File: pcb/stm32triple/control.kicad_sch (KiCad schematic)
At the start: 30 parts, among them J1 USB_C_Receptacle_USB2.0, P1 FTSH-107-01-L-DV-K, P2 ST-Link, P3 AFC07-S24FCC-00, SW1 RotaryEncoder_Switch, U1 STM32G431CBUx, U2 TPS82130, U3 BME680, U7 TSOP312xx, U8 TSOP312xx

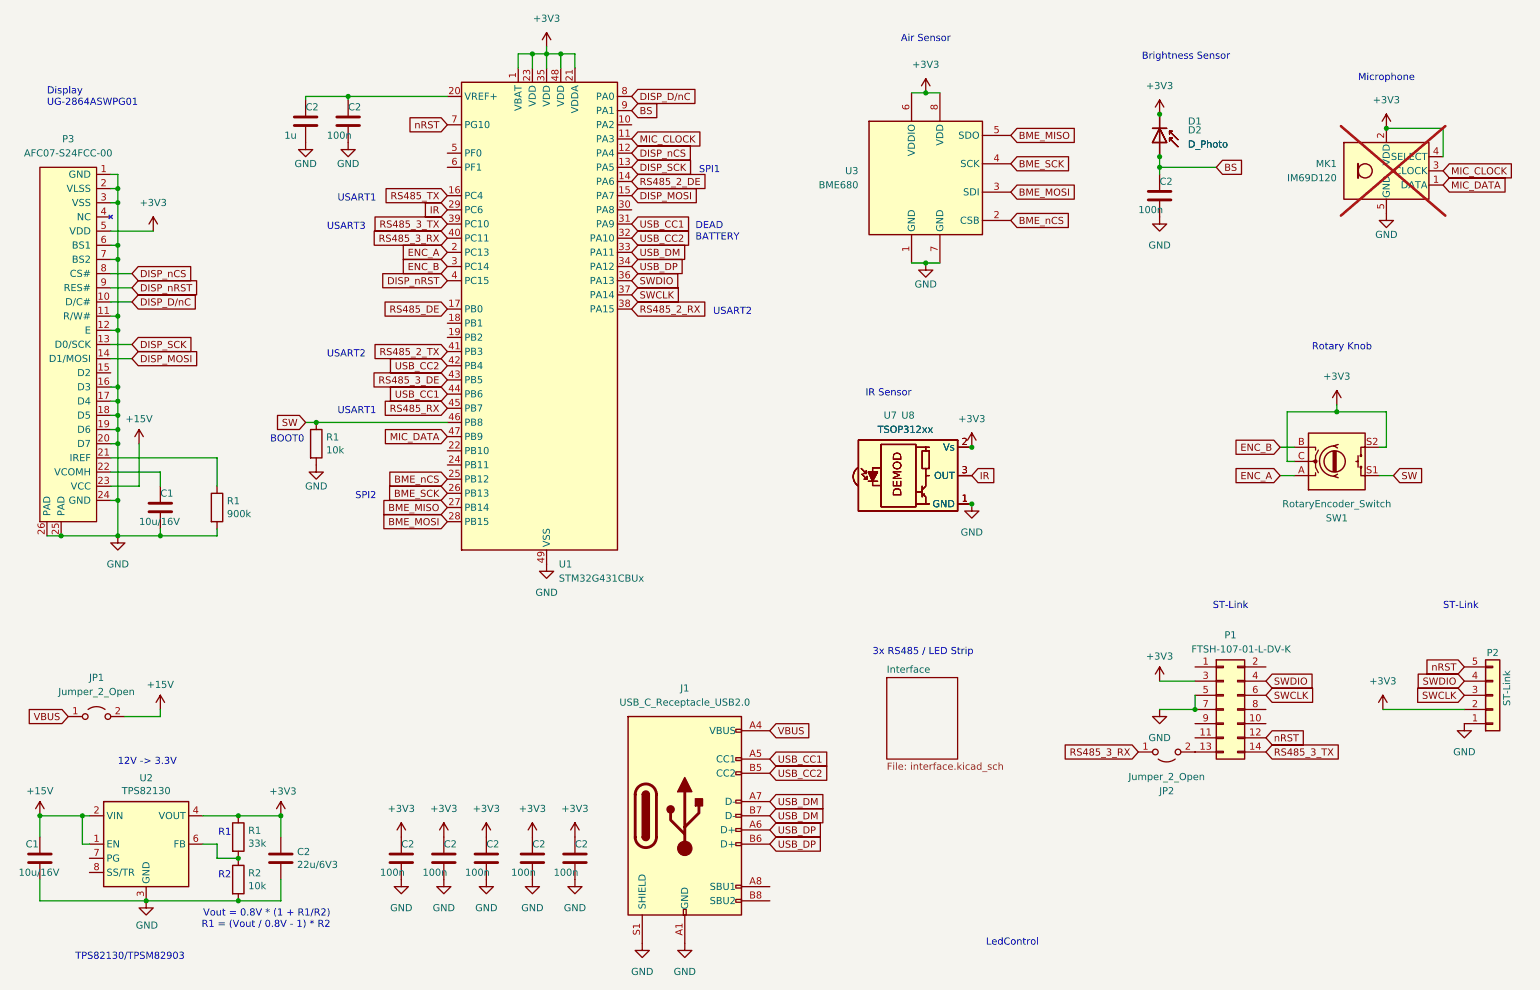
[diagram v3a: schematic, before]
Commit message: Use TSOP38338
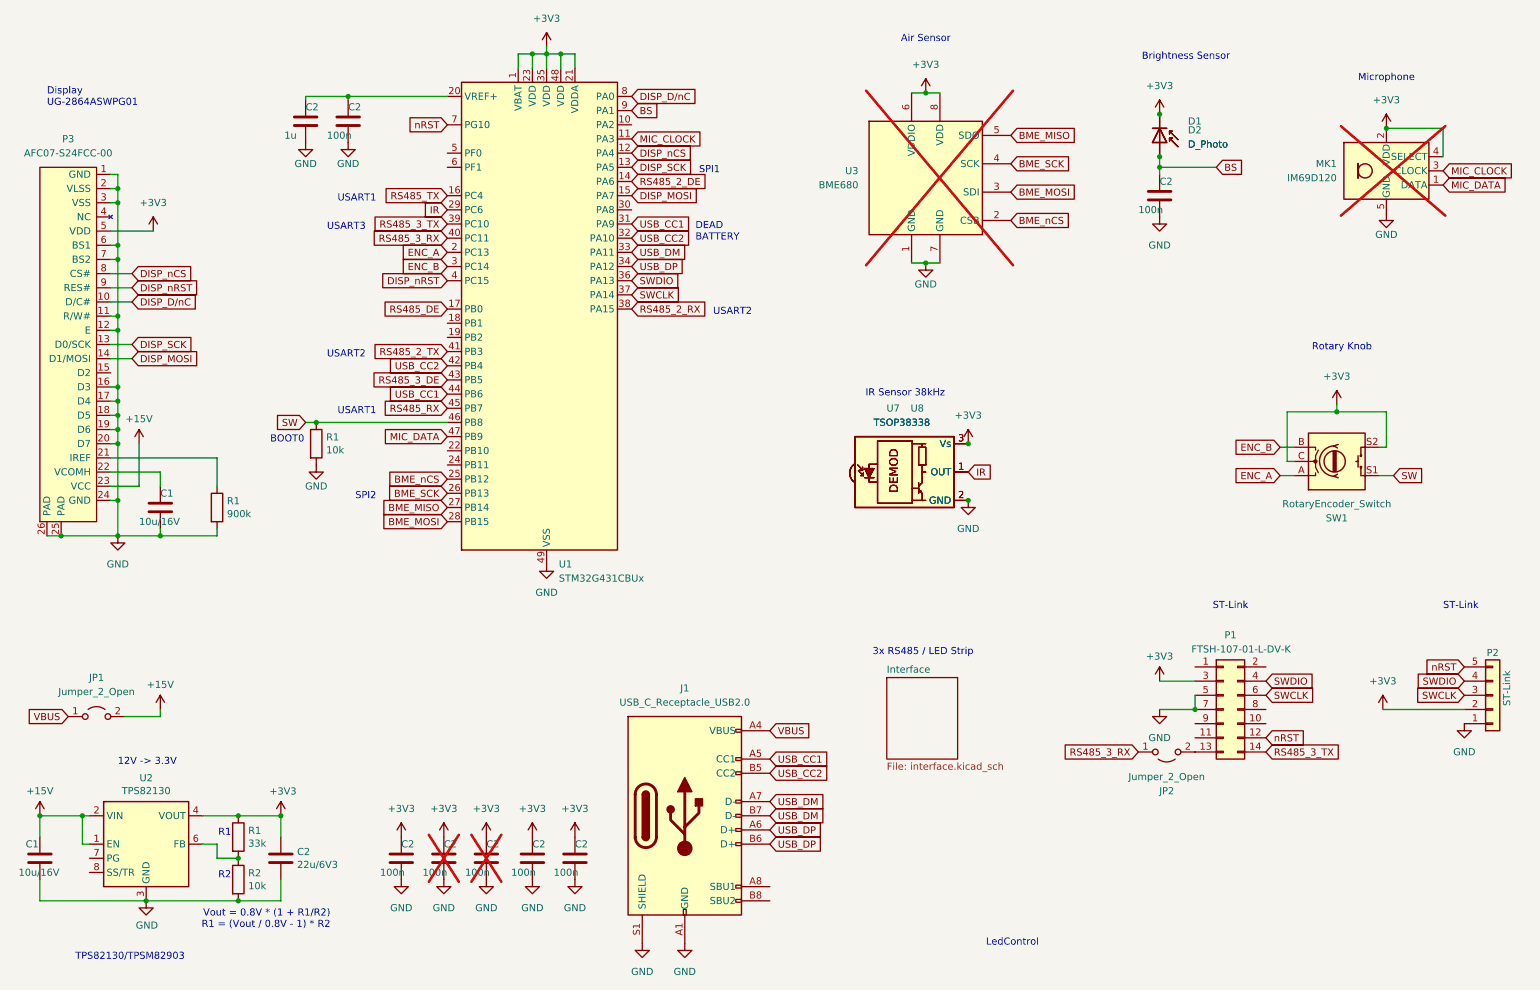
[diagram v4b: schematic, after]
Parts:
- removed U7, U8: TSOP312xx, local:TSOP31238, symbol Interface_Optical:TSOP312xx
- added U7, U8: TSOP38338, local:TSOP38338, symbol Interface_Optical:TSOP382xx
- C2: now not fitted
- J1: footprint local:USB4105-GF-A-120 -> local:TYPE-C-16PIN-2MD-073
- U1: footprint local:STM32G431CBU -> local:STM32-UFQFPN48
- U3: now not fitted; now in the parts list
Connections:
- net +3V3: now also U7.3 (Vs), U8.3 (Vs)
- net GND: now also U7.2 (GND), U8.2 (GND)
- net IR: now also U7.1 (OUT), U8.1 (OUT)
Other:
- note added: "IR Sensor 38kHz"
- note removed: "IR Sensor"
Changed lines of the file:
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@@
 	)
 	(junction
-		(at 186.055 111.125)
+		(at 19.05 167.005)
 		(diameter 0)
 		(color 0 0 0 0)
 	)
 	(junction
-		(at 19.05 167.005)
+		(at 219.71 48.895)
 		(diameter 0)
 		(color 0 0 0 0)
 	)
 	(junction
-		(at 219.71 48.895)
+		(at 185.42 110.49)
 		(diameter 0)
 		(color 0 0 0 0)
@@
 	)
 	(junction
-		(at 54.61 182.245)
+		(at 185.42 100.33)
 		(diameter 0)
 		(color 0 0 0 0)
 	)
 	(junction
-		(at 54.61 167.005)
+		(at 54.61 182.245)
 		(diameter 0)
 		(color 0 0 0 0)
 	)
 	(junction
-		(at 112.395 30.48)
+		(at 54.61 167.005)
 		(diameter 0)
 		(color 0 0 0 0)
 	)
 	(junction
-		(at 186.055 100.965)
+		(at 112.395 30.48)
 		(diameter 0)
 		(color 0 0 0 0)
@@
 		)
 	)
-	(text "IR Sensor"
+	(text "IR Sensor 38kHz"
 		(exclude_from_sim no)
 		(at 167.005 92.075 0)
@@
 	(global_label "IR"
 		(shape input)
-		(at 186.055 106.045 0)
+		(at 185.42 105.41 0)
 		(fields_autoplaced yes)
 		(effects
@@
 		)
 		(property "Intersheetrefs" "${INTERSHEET_REFS}"
-			(at 190.915 106.045 0)
+			(at 190.28 105.41 0)
 			(effects
 				(font
@@
 		(unit 1)
 		(exclude_from_sim no)
-		(in_bom no)
+		(in_bom yes)
 		(on_board yes)
-		(dnp no)
+		(dnp yes)
 		(fields_autoplaced yes)
 		(property "Reference" "U3"
@@
 	(symbol
 		(lib_id "power:GND")
-		(at 186.055 111.125 0)
+		(at 185.42 110.49 0)
 		(unit 1)
 		(exclude_from_sim no)
@@
 		(fields_autoplaced yes)
 		(property "Reference" "#PWR010"
-			(at 186.055 117.475 0)
+			(at 185.42 116.84 0)
 			(effects
 				(font
@@
 		)
 		(property "Value" "GND"
-			(at 186.055 116.205 0)
+			(at 185.42 115.57 0)
 			(effects
 				(font
@@
 		)
 		(property "Footprint" ""
-			(at 186.055 111.125 0)
+			(at 185.42 110.49 0)
 			(effects
 				(font
@@
 		)
 		(property "Datasheet" ""
-			(at 186.055 111.125 0)
+			(at 185.42 110.49 0)
 			(effects
 				(font
@@
 		)
 		(property "Description" ""
-			(at 186.055 111.125 0)
+			(at 185.42 110.49 0)
 			(effects
 				(font
@@
 			)
 		)
-		(property "Footprint" "local:STM32G431CBU"
+		(property "Footprint" "local:STM32-UFQFPN48"
 			(at 94.615 119.38 0)
 			(effects
@@
 		(in_bom yes)
 		(on_board yes)
-		(dnp no)
+		(dnp yes)
 		(property "Reference" "C2"
 			(at 91.44 172.085 0)
@@
 		(in_bom yes)
 		(on_board yes)
-		(dnp no)
+		(dnp yes)
 		(property "Reference" "C2"
 			(at 99.06 172.085 0)
@@
 	(symbol
 		(lib_id "power:+3V3")
-		(at 186.055 100.965 0)
+		(at 185.42 100.33 0)
 		(unit 1)
 		(exclude_from_sim no)
@@
 		(fields_autoplaced yes)
 		(property "Reference" "#PWR02"
-			(at 186.055 104.775 0)
+			(at 185.42 104.14 0)
 			(effects
 				(font
@@
 		)
 		(property "Value" "+3V3"
-			(at 186.055 95.885 0)
+			(at 185.42 95.25 0)
 			(effects
 				(font
@@
 		)
 		(property "Footprint" ""
-			(at 186.055 100.965 0)
+			(at 185.42 100.33 0)
 			(effects
 				(font
@@
 		)
 		(property "Datasheet" ""
-			(at 186.055 100.965 0)
+			(at 185.42 100.33 0)
 			(effects
 				(font
@@
 		)
 		(property "Description" ""
-			(at 186.055 100.965 0)
+			(at 185.42 100.33 0)
 			(effects
 				(font
@@
 	)
 	(symbol
+		(lib_id "Interface_Optical:TSOP382xx")
+		(at 175.26 105.41 0)
+		(unit 1)
+		(exclude_from_sim no)
+		(in_bom yes)
+		(on_board yes)
+		(dnp no)
+		(property "Reference" "U8"
+			(at 176.276 93.98 0)
+			(effects
+				(font
+					(size 1.27 1.27)
+				)
+			)
+		)
+		(property "Value" "TSOP38338"
+			(at 173.525 96.52 0)
+			(effects
+				(font
+					(size 1.27 1.27)
+				)
+			)
+		)
+		(property "Footprint" "local:TSOP38338"
+			(at 173.99 114.935 0)
+			(effects
+				(font
+					(size 1.27 1.27)
+				)
+				(hide yes)
+			)
+		)
+		(property "Datasheet" "http://www.vishay.com/docs/82491/tsop382.pdf"
+			(at 191.77 97.79 0)
+			(effects
+				(font
+					(size 1.27 1.27)
+				)
+				(hide yes)
+			)
+		)
+		(property "Description" "Photo Modules for PCM Remote Control Systems"
+			(at 175.26 105.41 0)
+			(effects
+				(font
+					(size 1.27 1.27)
+				)
+				(hide yes)
+			)
+		)
+		(pin "3"
+		)
+		(pin "1"
+		)
+		(pin "2"
+		)
+		(instances
+			(project "control"
+				(path "/4b540715-c4ed-4902-8525-92fb403f6b2e"
+					(reference "U8")
+					(unit 1)
+				)
+			)
+		)
+	)
+	(symbol
 		(lib_id "Connector_Generic:Conn_01x05")
 		(at 279.4 145.415 0)
@@
 	)
 	(symbol
-		(lib_id "Interface_Optical:TSOP312xx")
-		(at 175.895 106.045 0)
-		(unit 1)
-		(exclude_from_sim no)
-		(in_bom no)
-		(on_board yes)
-		(dnp no)
-		(property "Reference" "U7"
-			(at 171.45 95.25 0)
-			(effects
-				(font
-					(size 1.27 1.27)
-				)
-			)
-		)
-		(property "Value" "TSOP312xx"
-			(at 174.16 97.79 0)
-			(effects
-				(font
-					(size 1.27 1.27)
-				)
-			)
-		)
-		(property "Footprint" "local:TSOP31238"
-			(at 174.625 115.57 0)
-			(effects
-				(font
-					(size 1.27 1.27)
-				)
-				(hide yes)
-			)
-		)
-		(property "Datasheet" "http://www.vishay.com/docs/82492/tsop312.pdf"
-			(at 192.405 98.425 0)
-			(effects
-				(font
-					(size 1.27 1.27)
-				)
-				(hide yes)
-			)
-		)
-		(property "Description" ""
-			(at 175.895 106.045 0)
-			(effects
-				(font
-					(size 1.27 1.27)
-				)
-				(hide yes)
-			)
-		)
-		(pin "1"
-		)
-		(pin "2"
-		)
-		(pin "3"
-		)
-		(instances
-			(project "control"
-				(path "/4b540715-c4ed-4902-8525-92fb403f6b2e"
-					(reference "U7")
-					(unit 1)
-				)
-			)
-		)
-	)
-	(symbol
 		(lib_id "Device:C")
 		(at 62.23 174.625 0)
@@
 	)
 	(symbol
-		(lib_id "Interface_Optical:TSOP312xx")
-		(at 175.895 106.045 0)
+		(lib_id "Interface_Optical:TSOP382xx")
+		(at 175.26 105.41 0)
 		(unit 1)
 		(exclude_from_sim no)
-		(in_bom no)
+		(in_bom yes)
 		(on_board yes)
 		(dnp no)
-		(property "Reference" "U8"
-			(at 174.625 95.25 0)
+		(property "Reference" "U7"
+			(at 171.958 93.98 0)
 			(effects
 				(font
@@
 			)
 		)
-		(property "Value" "TSOP312xx"
-			(at 174.16 97.79 0)
+		(property "Value" "TSOP38338"
+			(at 173.525 96.52 0)
 			(effects
 				(font
@@
 			)
 		)
-		(property "Footprint" "local:TSOP31238"
-			(at 174.625 115.57 0)
+		(property "Footprint" "local:TSOP38338"
+			(at 173.99 114.935 0)
 			(effects
 				(font
@@
 			)
 		)
-		(property "Datasheet" "http://www.vishay.com/docs/82492/tsop312.pdf"
-			(at 192.405 98.425 0)
+		(property "Datasheet" "http://www.vishay.com/docs/82491/tsop382.pdf"
+			(at 191.77 97.79 0)
 			(effects
 				(font
@@
 			)
 		)
-		(property "Description" ""
-			(at 175.895 106.045 0)
+		(property "Description" "Photo Modules for PCM Remote Control Systems"
+			(at 175.26 105.41 0)
 			(effects
 				(font
@@
 			)
 		)
+		(pin "3"
+		)
 		(pin "1"
 		)
 		(pin "2"
 		)
-		(pin "3"
-		)
 		(instances
-			(project "control"
+			(project ""
 				(path "/4b540715-c4ed-4902-8525-92fb403f6b2e"
-					(reference "U8")
+					(reference "U7")
 					(unit 1)
 				)
@@
 			)
 		)
-		(property "Footprint" "local:USB4105-GF-A-120"
+		(property "Footprint" "local:TYPE-C-16PIN-2MD-073"
 			(at 138.43 167.005 0)
 			(effects
